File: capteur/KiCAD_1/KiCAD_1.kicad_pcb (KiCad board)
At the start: 2 copper layers, 68.6 x 60.6 mm, 25 parts, among them J1 Power, J2 Digital/PWM, J3 Analog, J4 Digital/PWM, U1 Bluetooth_HC05, U2 LTC1050CN8, U3 DM-OLED096-636, U4 Graphite_sensor, U5 Rotary_encoder_KY_040, U6 Potentionmeter_MCP41010, U7 Flex_sensor, U8 Servo_motor

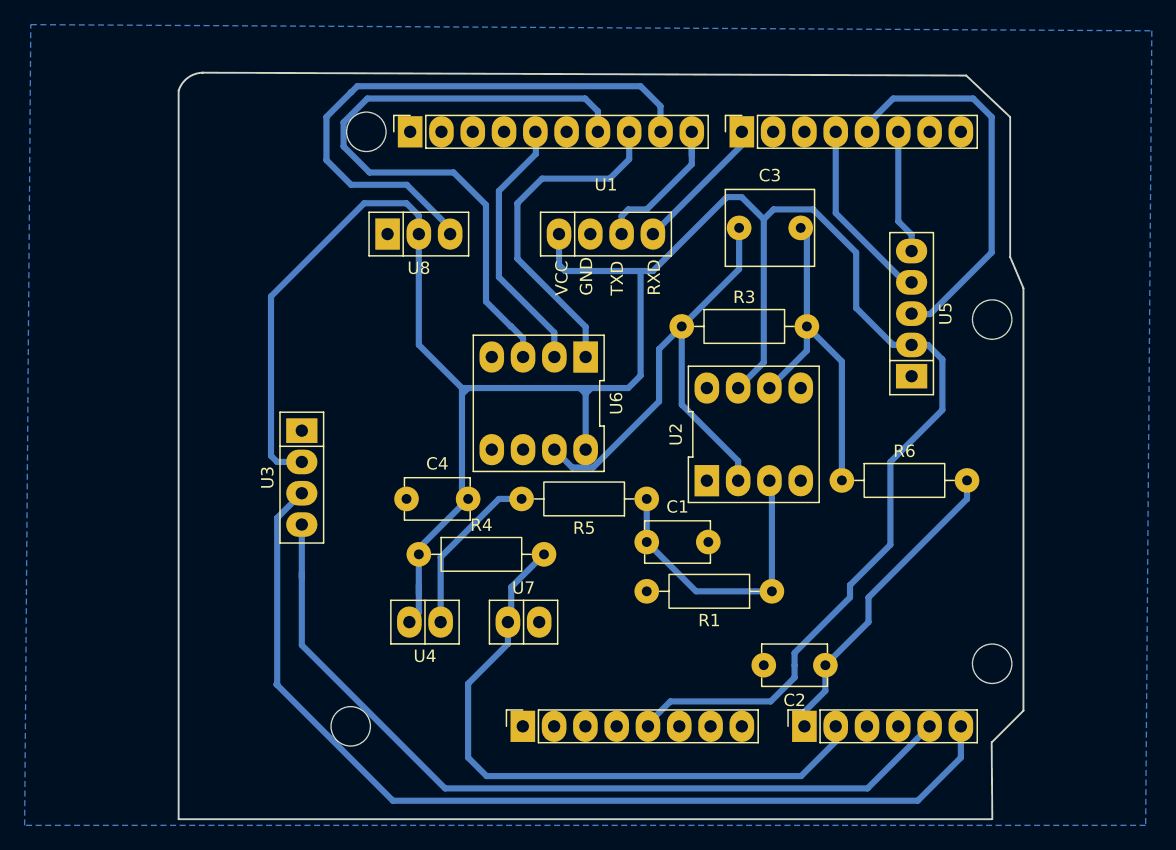
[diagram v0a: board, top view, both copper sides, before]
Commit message: final KICAD
Resolved the errors
Used a red cable to connect an isolated GND
Changed directory name to make it relative ${KIPRJMOD}
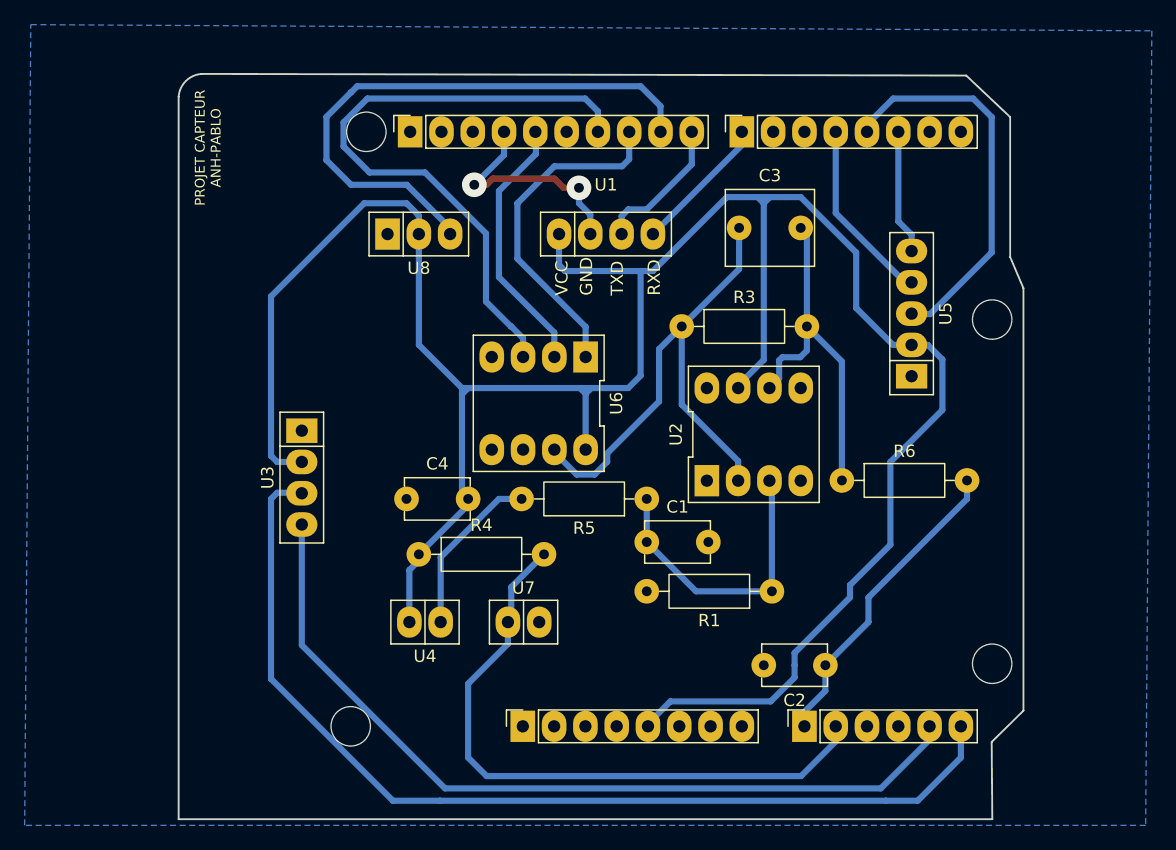
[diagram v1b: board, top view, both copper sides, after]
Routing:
- net GND: track 0.00 -> 18.4 mm, vias 0 -> 2
- net TXD: track 13.5 -> 11.5 mm
- net +5V: track 204.7 -> 206.6 mm
- net SCL: track 79.8 -> 81.4 mm
- net MOSI: track 54.2 -> 52.8 mm
- net Pot_1: track 42.5 -> 43.5 mm
- net Net-(U2-OUT): track 28.1 -> 29.0 mm
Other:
- board size 68.6 x 60.6 mm -> 68.6 x 60.5 mm
- board text added: "PROJET CAPTEUR ANH-PABLO"
